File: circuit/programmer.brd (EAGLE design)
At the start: 100 x 90 mm, 23 parts, among them U1 TEENSY_3.0_DIL, X1 ESP01, X2 DIRTCHEAPRX-PROG-MINI, X3 DIRTCHEAPRX-PROG-NANO, X4 ESP01

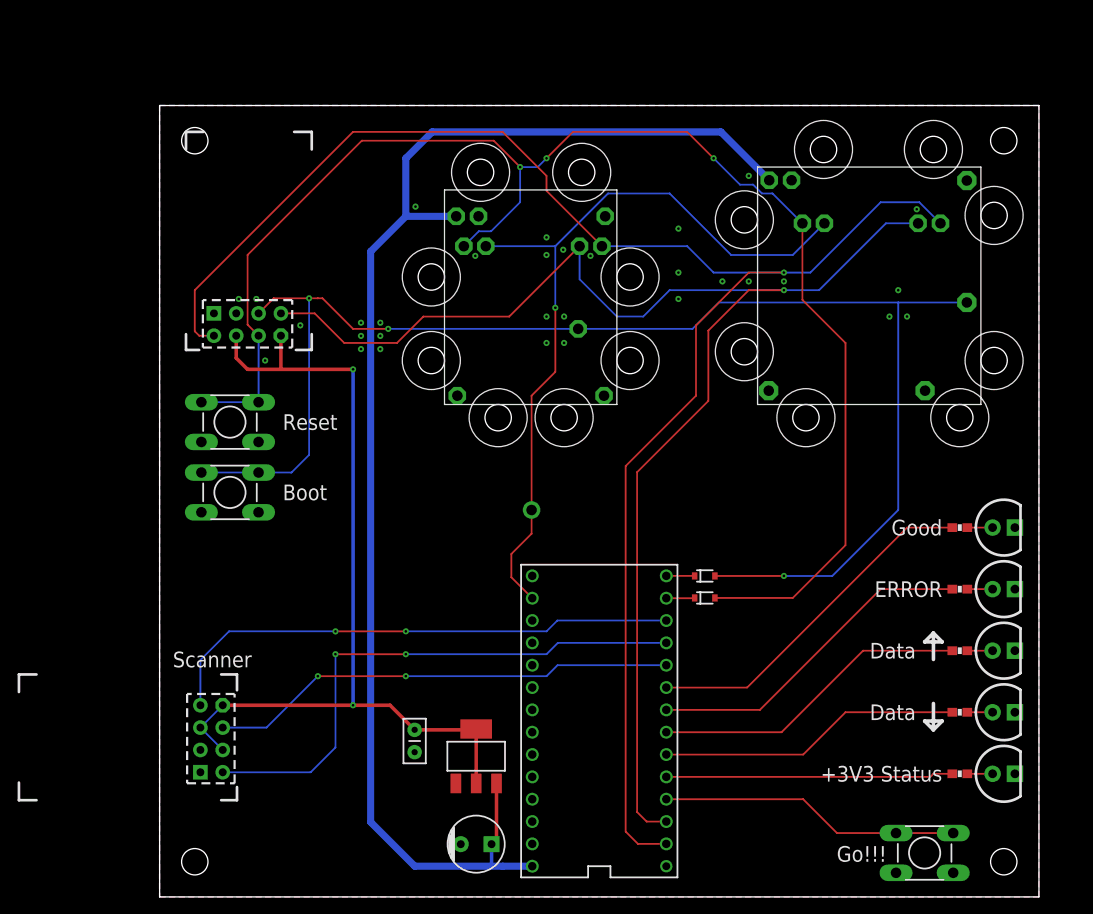
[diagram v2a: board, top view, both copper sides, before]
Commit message: programmer, more vias, disconnectable boot signal
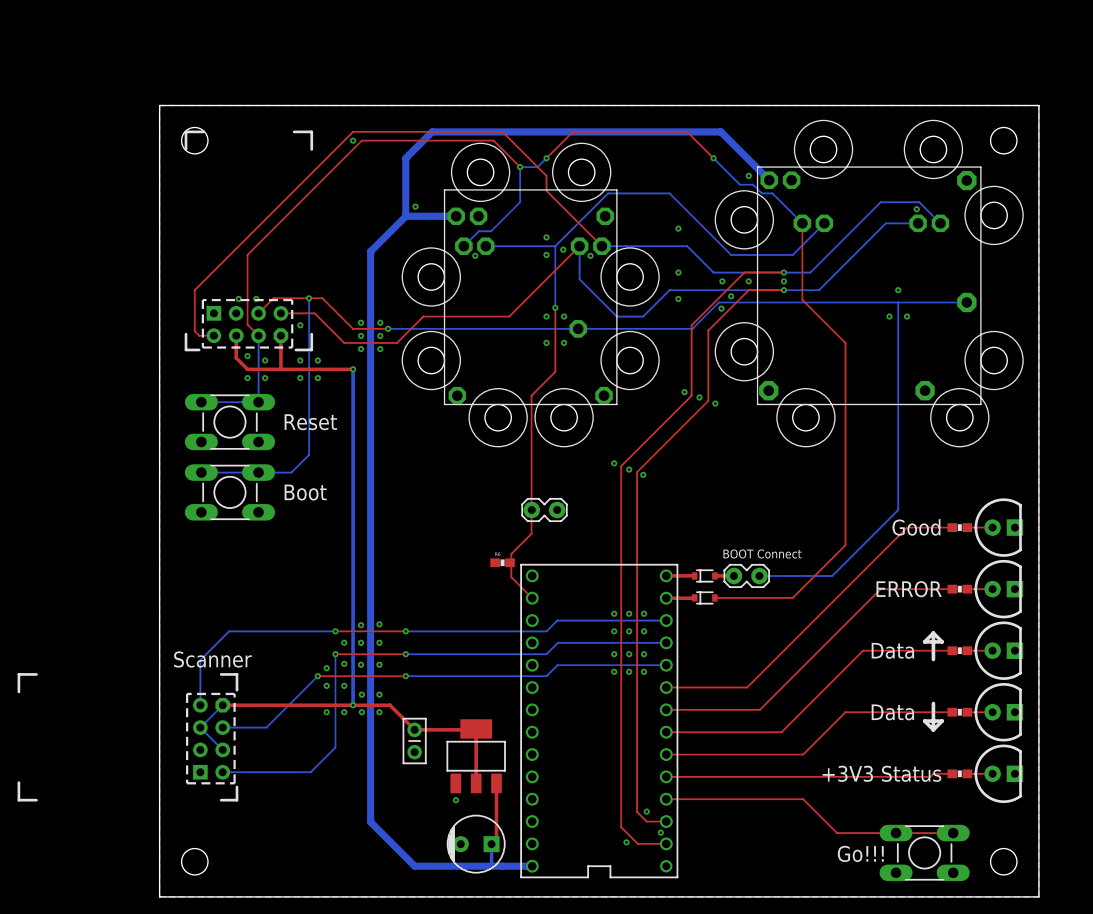
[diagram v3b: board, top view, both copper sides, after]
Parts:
- added JP1, JP2: (no value), dirtcheaprx:1X02_LOCK
- added R6: (no value), dirtcheaprx:0603-RES
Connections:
- new net N$8: D2.2, JP1.1
- net A0: now also JP2.1, R6.2
- net BOOT: now also JP1.2; no longer D2.2
- net GND: now also JP2.2, R6.1, U1.15/A1, U1.16/A2, U1.17/A3, U1.18/A4
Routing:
- net BOOT: track 162.4 -> 157.3 mm, vias 3 -> 2
- net N$8: track 0.00 -> 2.17 mm
- net TX: track 189.8 -> 190.5 mm
- net A0: track 88.5 -> 88.6 mm, vias 2 -> 1
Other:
- board text added: "BOOT Connect"
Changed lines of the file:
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@@
 <text x="14" y="46" size="1.778" layer="21" font="vector" ratio="10" align="center-left">Boot</text>
 <text x="1.5" y="27" size="1.778" layer="21" font="vector" ratio="10" align="center-left">Scanner</text>
+<text x="64" y="38.5" size="1" layer="21">BOOT Connect</text>
 </plain>
 <attributes>
@@
 <attribute name="VALUE" x="26.46" y="20.27" size="0.6096" layer="27" rot="R270"/>
 </element>
+<element name="JP1" library="dirtcheaprx" package="1X02_LOCK" value="" x="65.5" y="36.5" smashed="yes">
+<attribute name="VALUE" x="64.23" y="33.325" size="1.27" layer="27"/>
+</element>
+<element name="R6" library="dirtcheaprx" package="0603-RES" value="" x="39" y="38" smashed="yes">
+<attribute name="NAME" x="38.111" y="38.762" size="0.4064" layer="25" font="vector"/>
+<attribute name="VALUE" x="37.984" y="36.857" size="0.4064" layer="27" font="vector"/>
+</element>
+<element name="JP2" library="dirtcheaprx" package="1X02_LOCK" value="" x="42.5" y="44" smashed="yes">
+<attribute name="VALUE" x="41.23" y="40.825" size="1.27" layer="27"/>
+</element>
 </elements>
 <signals>
@@
 <contactref element="U1" pad="0"/>
 <wire x1="57.62" y1="6.03" x2="54.393159375" y2="6.03" width="0.2032" layer="1"/>
-<wire x1="54.393159375" y1="6.03" x2="53" y2="7.423159375" width="0.2032" layer="1"/>
-<wire x1="53" y1="7.423159375" x2="53" y2="49" width="0.2032" layer="1"/>
+<wire x1="54.393159375" y1="6.03" x2="52.5" y2="7.923159375" width="0.2032" layer="1"/>
+<wire x1="52.5" y1="7.923159375" x2="52.5" y2="49" width="0.2032" layer="1"/>
 <wire x1="4" y1="69" x2="4" y2="64.323003125" width="0.2032" layer="1"/>
 <wire x1="4" y1="64.323003125" x2="4.500503125" y2="63.8225" width="0.2032" layer="1"/>
@@
 <wire x1="44" y1="82" x2="44" y2="80.3" width="0.2032" layer="1"/>
 <wire x1="44" y1="80.3" x2="50.3" y2="74" width="0.2032" layer="1"/>
-<wire x1="53" y1="49" x2="61" y2="57" width="0.2032" layer="1"/>
-<wire x1="61" y1="57" x2="61" y2="65" width="0.2032" layer="1"/>
-<wire x1="61" y1="65" x2="67" y2="71" width="0.2032" layer="1"/>
-<wire x1="67" y1="71" x2="71" y2="71" width="0.2032" layer="1"/>
+<wire x1="52.5" y1="49" x2="60.5" y2="57" width="0.2032" layer="1"/>
+<wire x1="60.5" y1="57" x2="60.5" y2="65" width="0.2032" layer="1"/>
+<wire x1="60.5" y1="65" x2="66.5" y2="71" width="0.2032" layer="1"/>
+<wire x1="66.5" y1="71" x2="71" y2="71" width="0.2032" layer="1"/>
 <via x="71" y="71" extent="1-16" drill="0.3" shape="octagon"/>
 <wire x1="71" y1="71" x2="74" y2="71" width="0.2032" layer="16"/>
@@
 <wire x1="26" y1="64.6" x2="22" y2="64.6" width="0.2032" layer="1"/>
 <wire x1="22" y1="64.6" x2="18.52188125" y2="68.07811875" width="0.2032" layer="1"/>
-<wire x1="18.52188125" y1="68.07811875" x2="18" y2="68.07811875" width="0.2032" layer="1"/>
 <wire x1="17" y1="68.07811875" x2="12.97061875" y2="68.07811875" width="0.2032" layer="1"/>
 <wire x1="12.97061875" y1="68.07811875" x2="11.255" y2="66.3625" width="0.2032" layer="1"/>
 <wire x1="76.5" y1="36.5" x2="84" y2="44" width="0.2032" layer="16"/>
 <wire x1="84" y1="44" x2="84" y2="67.6" width="0.2032" layer="16"/>
-<contactref element="D2" pad="2"/>
-<wire x1="63.15" y1="36.5" x2="71" y2="36.5" width="0.2032" layer="1"/>
-<via x="71" y="36.5" extent="1-16" drill="0.3" shape="octagon"/>
-<wire x1="71" y1="36.5" x2="76.5" y2="36.5" width="0.2032" layer="16"/>
+<wire x1="68.2178" y1="36.5" x2="76.5" y2="36.5" width="0.2032" layer="16"/>
 <contactref element="S3" pad="1"/>
 <contactref element="S3" pad="2"/>
@@
 <wire x1="17" y1="50.266965625" x2="17" y2="68.07811875" width="0.2032" layer="16"/>
 <via x="17" y="68.07811875" extent="1-16" drill="0.3" shape="octagon"/>
-<wire x1="17" y1="68.07811875" x2="18" y2="68.07811875" width="0.2032" layer="1"/>
+<wire x1="17" y1="68.07811875" x2="18.52188125" y2="68.07811875" width="0.2032" layer="1"/>
+<contactref element="JP1" pad="2"/>
 </signal>
 <signal name="GND">
@@
 <via x="22.9" y="65.3" extent="1-16" drill="0.3" shape="octagon"/>
 <via x="25.1" y="65.3" extent="1-16" drill="0.3" shape="octagon"/>
+<via x="57" y="7.3" extent="1-16" drill="0.3" shape="octagon"/>
+<via x="55.4" y="9.7" extent="1-16" drill="0.3" shape="octagon"/>
+<via x="53.1" y="6.2" extent="1-16" drill="0.3" shape="octagon"/>
+<via x="53.4" y="25.6" extent="1-16" drill="0.3" shape="octagon"/>
+<via x="53.4" y="27.6" extent="1-16" drill="0.3" shape="octagon"/>
+<via x="53.4" y="30.2" extent="1-16" drill="0.3" shape="octagon"/>
+<via x="53.4" y="32.2" extent="1-16" drill="0.3" shape="octagon"/>
+<via x="51.7" y="32.2" extent="1-16" drill="0.3" shape="octagon"/>
+<via x="51.7" y="30.2" extent="1-16" drill="0.3" shape="octagon"/>
+<via x="51.7" y="27.6" extent="1-16" drill="0.3" shape="octagon"/>
+<via x="51.7" y="25.6" extent="1-16" drill="0.3" shape="octagon"/>
+<via x="55.1" y="25.6" extent="1-16" drill="0.3" shape="octagon"/>
+<via x="55.1" y="27.6" extent="1-16" drill="0.3" shape="octagon"/>
+<via x="55.1" y="32.2" extent="1-16" drill="0.3" shape="octagon"/>
+<via x="55.1" y="30.2" extent="1-16" drill="0.3" shape="octagon"/>
+<contactref element="U1" pad="15/A1"/>
+<contactref element="U1" pad="18/A4"/>
+<contactref element="U1" pad="17/A3"/>
+<contactref element="U1" pad="16/A2"/>
+<contactref element="R6" pad="1"/>
+<contactref element="JP2" pad="2"/>
+<via x="22" y="86" extent="1-16" drill="0.3" shape="octagon"/>
+<via x="65" y="68.3" extent="1-16" drill="0.3" shape="octagon"/>
+<via x="63.9" y="66.9" extent="1-16" drill="0.3" shape="octagon"/>
+<via x="61.4" y="56.8" extent="1-16" drill="0.3" shape="octagon"/>
+<via x="53.4" y="48.6" extent="1-16" drill="0.3" shape="octagon"/>
+<via x="55" y="48" extent="1-16" drill="0.3" shape="octagon"/>
+<via x="59.7" y="57.4" extent="1-16" drill="0.3" shape="octagon"/>
+<via x="63.2" y="56.1" extent="1-16" drill="0.3" shape="octagon"/>
+<via x="51.7" y="49.3" extent="1-16" drill="0.3" shape="octagon"/>
+<via x="23" y="23" extent="1-16" drill="0.3" shape="octagon"/>
+<via x="25" y="23" extent="1-16" drill="0.3" shape="octagon"/>
+<via x="25" y="21" extent="1-16" drill="0.3" shape="octagon"/>
+<via x="23" y="21" extent="1-16" drill="0.3" shape="octagon"/>
+<via x="22.9" y="26.4" extent="1-16" drill="0.3" shape="octagon"/>
+<via x="22.9" y="28.9" extent="1-16" drill="0.3" shape="octagon"/>
+<via x="22.9" y="30.9" extent="1-16" drill="0.3" shape="octagon"/>
+<via x="25" y="31" extent="1-16" drill="0.3" shape="octagon"/>
+<via x="25" y="28.9" extent="1-16" drill="0.3" shape="octagon"/>
+<via x="25" y="26.4" extent="1-16" drill="0.3" shape="octagon"/>
+<via x="21" y="26.5" extent="1-16" drill="0.3" shape="octagon"/>
+<via x="21" y="28.9" extent="1-16" drill="0.3" shape="octagon"/>
+<via x="21" y="24" extent="1-16" drill="0.3" shape="octagon"/>
+<via x="19" y="24" extent="1-16" drill="0.3" shape="octagon"/>
+<via x="19" y="26" extent="1-16" drill="0.3" shape="octagon"/>
+<via x="19" y="21" extent="1-16" drill="0.3" shape="octagon"/>
+<via x="21" y="21" extent="1-16" drill="0.3" shape="octagon"/>
+<via x="33.7" y="11" extent="1-16" drill="0.3" shape="octagon"/>
+<via x="16" y="61" extent="1-16" drill="0.3" shape="octagon"/>
+<via x="18" y="61" extent="1-16" drill="0.3" shape="octagon"/>
+<via x="18" y="59" extent="1-16" drill="0.3" shape="octagon"/>
+<via x="16" y="59" extent="1-16" drill="0.3" shape="octagon"/>
+<via x="12" y="59" extent="1-16" drill="0.3" shape="octagon"/>
+<via x="10" y="59" extent="1-16" drill="0.3" shape="octagon"/>
+<via x="10" y="61.5" extent="1-16" drill="0.3" shape="octagon"/>
 </signal>
 <signal name="A0">
@@
 <wire x1="45" y1="67" x2="45" y2="59.7" width="0.2032" layer="1"/>
 <wire x1="45" y1="59.7" x2="42.3" y2="57" width="0.2032" layer="1"/>
+<wire x1="42.3" y1="41.3" x2="40" y2="39" width="0.2032" layer="1"/>
+<wire x1="40" y1="36.35" x2="42.38" y2="33.97" width="0.2032" layer="1"/>
+<contactref element="R6" pad="2"/>
+<wire x1="40" y1="39" x2="40" y2="38" width="0.2032" layer="1"/>
+<wire x1="40" y1="36.35" x2="40" y2="38" width="0.2032" layer="1"/>
+<wire x1="40" y1="38" x2="39.85" y2="38" width="0.2032" layer="1"/>
+<contactref element="JP2" pad="1"/>
 <wire x1="42.3" y1="57" x2="42.3" y2="44" width="0.2032" layer="1"/>
-<wire x1="42.3" y1="44" x2="42.3" y2="41.3" width="0.2032" layer="1"/>
-<wire x1="42.3" y1="41.3" x2="40" y2="39" width="0.2032" layer="1"/>
-<wire x1="40" y1="39" x2="40" y2="36.35" width="0.2032" layer="1"/>
-<wire x1="40" y1="36.35" x2="42.38" y2="33.97" width="0.2032" layer="1"/>
-<via x="42.3" y="44" extent="1-16" drill="1.2" diameter="2" shape="octagon"/>
+<wire x1="42.3" y1="41.3" x2="42.3" y2="44" width="0.2032" layer="1"/>
+<wire x1="42.3" y1="44" x2="42.3222" y2="44" width="0.2032" layer="1"/>
 </signal>
 <signal name="VIN">
@@
 <contactref element="U1" pad="11"/>
 <contactref element="D1" pad="1"/>
-<wire x1="57.62" y1="33.97" x2="60.85" y2="33.97" width="0.2032" layer="1"/>
+<wire x1="57.62" y1="33.97" x2="60.85" y2="33.97" width="0.4064" layer="1"/>
 <wire x1="60.85" y1="33.97" x2="60.85" y2="34" width="0.2032" layer="1"/>
 </signal>
@@
 <contactref element="U1" pad="12"/>
 <contactref element="D2" pad="1"/>
-<wire x1="57.62" y1="36.51" x2="60.85" y2="36.51" width="0.2032" layer="1"/>
+<wire x1="57.62" y1="36.51" x2="60.85" y2="36.51" width="0.4064" layer="1"/>
 <wire x1="60.85" y1="36.51" x2="60.85" y2="36.5" width="0.2032" layer="1"/>
 </signal>
@@
 <contactref element="U1" pad="3.3V"/>
 </signal>
+<signal name="N$8">
+<contactref element="D2" pad="2"/>
+<contactref element="JP1" pad="1"/>
+<wire x1="63.15" y1="36.5" x2="65.3222" y2="36.5" width="0.4064" layer="1"/>
+</signal>
 </signals>

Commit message: gerber out, added some optional pull-up resistors
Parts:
- added R7, R8: (no value), dirtcheaprx:0603-RES
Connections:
- removed net +3V3: C2.1, IC1.2, IC1.4, X1.CH_PD, X1.VCC, X4.CH_PD, X4.GPIO0, X4.VCC
- net 3.3V: now also C2.1, IC1.2, IC1.4, R7.2, R8.2, X1.CH_PD, X1.VCC, X4.CH_PD, X4.GPIO0, X4.VCC
- net BOOT: now also R7.1
- net RST: now also R8.1
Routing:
- net 3.3V: track 0.00 -> 113.6 mm, vias 0 -> 2
- net +3V3: track 101.8 -> 0.00 mm, vias 2 -> 0
- net BOOT: track 157.3 -> 161.0 mm
- net RST: track 167.9 -> 171.5 mm, vias 3 -> 4
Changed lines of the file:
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@@
 </element>
 <element name="R6" library="dirtcheaprx" package="0603-RES" value="" x="39" y="38" smashed="yes">
-<attribute name="NAME" x="38.111" y="38.762" size="0.4064" layer="25" font="vector"/>
 <attribute name="VALUE" x="37.984" y="36.857" size="0.4064" layer="27" font="vector"/>
 </element>
@@
 <attribute name="VALUE" x="41.23" y="40.825" size="1.27" layer="27"/>
 </element>
+<element name="R7" library="dirtcheaprx" package="0603-RES" value="" x="15.5" y="48.5" smashed="yes">
+<attribute name="VALUE" x="14.484" y="47.357" size="0.4064" layer="27" font="vector"/>
+</element>
+<element name="R8" library="dirtcheaprx" package="0603-RES" value="" x="15.5" y="56.5" smashed="yes">
+<attribute name="VALUE" x="14.484" y="55.357" size="0.4064" layer="27" font="vector"/>
+</element>
 </elements>
 <signals>
-<signal name="+3V3">
-<contactref element="X1" pad="VCC"/>
-<contactref element="X1" pad="CH_PD"/>
-<wire x1="13.795" y1="60" x2="13.795" y2="63.8225" width="0.4064" layer="1"/>
-<wire x1="8.715" y1="63.8225" x2="8.715" y2="61.285" width="0.4064" layer="1"/>
-<wire x1="8.715" y1="61.285" x2="10" y2="60" width="0.4064" layer="1"/>
-<wire x1="10" y1="60" x2="13.795" y2="60" width="0.4064" layer="1"/>
-<wire x1="13.795" y1="60" x2="22" y2="60" width="0.4064" layer="1"/>
-<via x="22" y="60" extent="1-16" drill="0.3" shape="octagon"/>
-<wire x1="22" y1="60" x2="22" y2="21.795" width="0.4064" layer="16"/>
-<contactref element="X4" pad="GPIO0"/>
-<contactref element="X4" pad="VCC"/>
-<contactref element="X4" pad="CH_PD"/>
-<wire x1="7.1775" y1="21.795" x2="22" y2="21.795" width="0.4064" layer="1"/>
-<via x="22" y="21.795" extent="1-16" drill="0.3" shape="octagon"/>
-<wire x1="7.1775" y1="21.795" x2="4.6375" y2="19.255" width="0.2032" layer="16"/>
-<wire x1="7.1775" y1="16.715" x2="4.6375" y2="19.255" width="0.2032" layer="16"/>
-<contactref element="IC1" pad="4"/>
-<contactref element="C2" pad="1"/>
-<contactref element="IC1" pad="2"/>
-<wire x1="29" y1="19" x2="36" y2="19" width="0.4064" layer="1"/>
-<wire x1="36" y1="19" x2="36" y2="19.099" width="0.4064" layer="1"/>
-<wire x1="36" y1="12.9012" x2="36" y2="19.099" width="0.4064" layer="1"/>
-<wire x1="22" y1="21.795" x2="26.205" y2="21.795" width="0.4064" layer="1"/>
-<wire x1="26.205" y1="21.795" x2="29" y2="19" width="0.4064" layer="1"/>
-</signal>
 <signal name="TX">
 <contactref element="X1" pad="TX"/>
@@
 <wire x1="11.255" y1="56.2606" x2="11.2512" y2="56.2606" width="0.2032" layer="16"/>
 <wire x1="11.2512" y1="56.2606" x2="4.7488" y2="56.2606" width="0.2032" layer="16"/>
+<contactref element="R8" pad="1"/>
+<via x="11.255" y="56.2606" extent="1-16" drill="0.3" shape="square"/>
+<wire x1="11.255" y1="56.2606" x2="14.65" y2="56.2606" width="0.254" layer="1"/>
+<wire x1="14.65" y1="56.2606" x2="14.65" y2="56.5" width="0.254" layer="1"/>
 </signal>
 <signal name="RX">
@@
 <wire x1="17" y1="68.07811875" x2="18.52188125" y2="68.07811875" width="0.2032" layer="1"/>
 <contactref element="JP1" pad="2"/>
+<contactref element="R7" pad="1"/>
+<wire x1="14.65" y1="48.5" x2="14.65" y2="48.2606" width="0.254" layer="1"/>
+<wire x1="14.65" y1="48.2606" x2="11.2512" y2="48.2606" width="0.254" layer="1"/>
 </signal>
 <signal name="GND">
@@
 <via x="10" y="59" extent="1-16" drill="0.3" shape="octagon"/>
 <via x="10" y="61.5" extent="1-16" drill="0.3" shape="octagon"/>
+<via x="77" y="40.5" extent="1-16" drill="0.3" shape="octagon"/>
+<via x="79" y="40.5" extent="1-16" drill="0.3" shape="octagon"/>
+<via x="76.2" y="37.2" extent="1-16" drill="0.3" shape="octagon"/>
+<via x="82" y="40.5" extent="1-16" drill="0.3" shape="octagon"/>
+<via x="85" y="40.5" extent="1-16" drill="0.3" shape="octagon"/>
+<via x="74.5" y="70" extent="1-16" drill="0.3" shape="octagon"/>
+<via x="77.5" y="70" extent="1-16" drill="0.3" shape="octagon"/>
+<via x="74.5" y="73" extent="1-16" drill="0.3" shape="octagon"/>
+<via x="71" y="75" extent="1-16" drill="0.3" shape="octagon"/>
+<via x="59.5" y="65.5" extent="1-16" drill="0.3" shape="octagon"/>
+<via x="59.5" y="63.5" extent="1-16" drill="0.3" shape="octagon"/>
 </signal>
 <signal name="A0">
@@
 <signal name="3.3V">
 <contactref element="U1" pad="3.3V"/>
+<contactref element="R8" pad="2"/>
+<contactref element="R7" pad="2"/>
+<contactref element="X1" pad="VCC"/>
+<contactref element="X1" pad="CH_PD"/>
+<wire x1="13.795" y1="60" x2="13.795" y2="63.8225" width="0.4064" layer="1"/>
+<wire x1="8.715" y1="63.8225" x2="8.715" y2="61.285" width="0.4064" layer="1"/>
+<wire x1="8.715" y1="61.285" x2="10" y2="60" width="0.4064" layer="1"/>
+<wire x1="10" y1="60" x2="13.795" y2="60" width="0.4064" layer="1"/>
+<wire x1="13.795" y1="60" x2="17" y2="60" width="0.4064" layer="1"/>
+<via x="22" y="60" extent="1-16" drill="0.3" shape="octagon"/>
+<wire x1="17" y1="60" x2="22" y2="60" width="0.4064" layer="1"/>
+<wire x1="22" y1="60" x2="22" y2="21.795" width="0.4064" layer="16"/>
+<contactref element="X4" pad="GPIO0"/>
+<contactref element="X4" pad="VCC"/>
+<contactref element="X4" pad="CH_PD"/>
+<wire x1="7.1775" y1="21.795" x2="22" y2="21.795" width="0.4064" layer="1"/>
+<via x="22" y="21.795" extent="1-16" drill="0.3" shape="octagon"/>
+<wire x1="7.1775" y1="21.795" x2="4.6375" y2="19.255" width="0.2032" layer="16"/>
+<wire x1="7.1775" y1="16.715" x2="4.6375" y2="19.255" width="0.2032" layer="16"/>
+<contactref element="IC1" pad="4"/>
+<contactref element="C2" pad="1"/>
+<contactref element="IC1" pad="2"/>
+<wire x1="29" y1="19" x2="36" y2="19" width="0.4064" layer="1"/>
+<wire x1="36" y1="19" x2="36" y2="19.099" width="0.4064" layer="1"/>
+<wire x1="36" y1="12.9012" x2="36" y2="19.099" width="0.4064" layer="1"/>
+<wire x1="22" y1="21.795" x2="26.205" y2="21.795" width="0.4064" layer="1"/>
+<wire x1="26.205" y1="21.795" x2="29" y2="19" width="0.4064" layer="1"/>
+<wire x1="16.35" y1="48.5" x2="16.35" y2="56.5" width="0.254" layer="1"/>
+<wire x1="16.35" y1="56.5" x2="17" y2="57.15" width="0.254" layer="1"/>
+<wire x1="17" y1="57.15" x2="17" y2="60" width="0.254" layer="1"/>
+<wire x1="36" y1="12.9012" x2="42.38" y2="8.57" width="0" layer="19" extent="1-1"/>
 </signal>
 <signal name="N$8">
